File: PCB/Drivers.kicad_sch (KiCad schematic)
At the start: 5 parts, among them U4 ISO1042DWVR

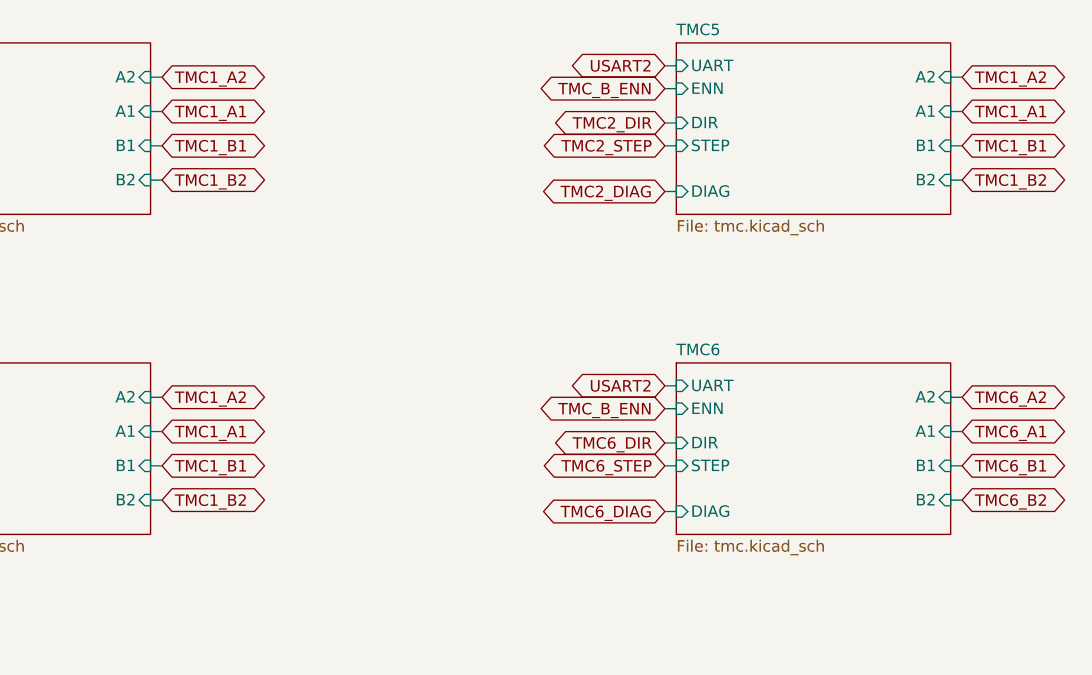
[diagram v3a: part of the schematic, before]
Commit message: Continued PCB Development - Routed MCU decoupeling and Isolated Crystal - Routed LDO Buck converter (VBUS (+5V) -> +3V3) - Routed Buck Converter (+24V -> +3V3) needs review (U2-pin1-GND) - Started Routing TMC2209 to their terminal blocks - Noticed issue with Stepper Lines coupeling back into +24V - TODO: Move Motor Input farther inside and add grounding isolation - Fixed Polariy mismatch with J3 (XT60 Battery Connector)
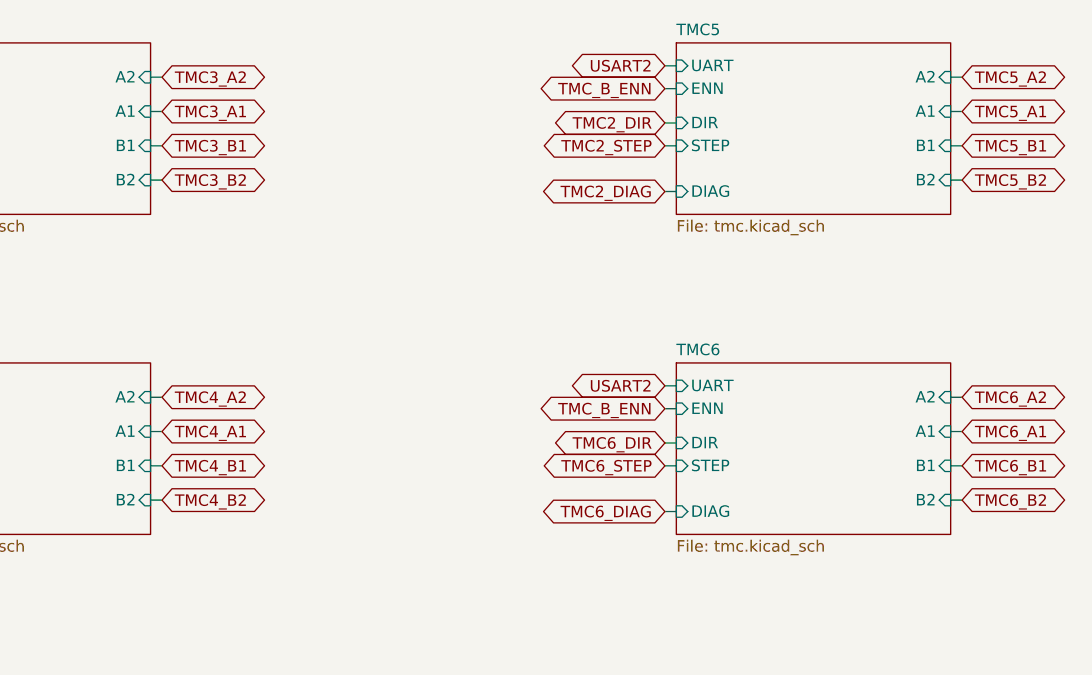
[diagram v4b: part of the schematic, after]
